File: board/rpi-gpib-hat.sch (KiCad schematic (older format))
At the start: 6 parts, among them J1 RPI_GPIO, J2 GPIB

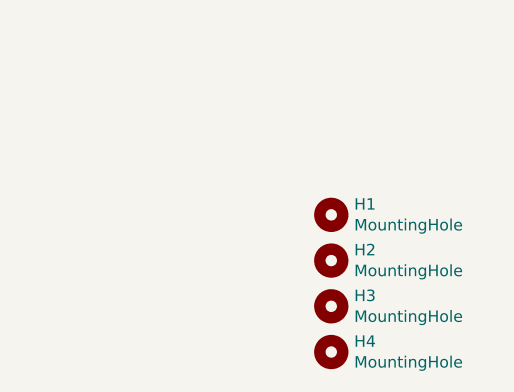
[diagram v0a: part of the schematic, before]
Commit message: Fix mounting holes to meet uHat spec.
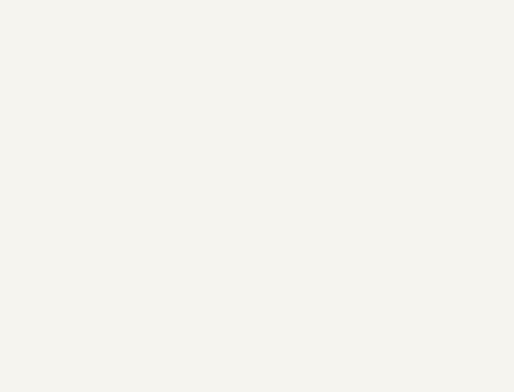
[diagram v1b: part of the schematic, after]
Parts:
- removed H1, H2, H3, H4: MountingHole, lib:MountingHole_2.7mm_M2.5_uHAT_RPi, symbol Mechanical:MountingHole
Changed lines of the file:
@@
 GPIO21
-$Comp
-L Mechanical:MountingHole H1
-U 1 1 5C7C4C81
-P 6150 6900
-F 0 "H1" H 6250 6946 50  0000 L CNN
-F 1 "MountingHole" H 6250 6855 50  0000 L CNN
-F 2 "lib:MountingHole_2.7mm_M2.5_uHAT_RPi" H 6150 6900 50  0001 C CNN
-F 3 "~" H 6150 6900 50  0001 C CNN
-	1    6150 6900
-	1    0    0    -1
-$EndComp
-$Comp
-L Mechanical:MountingHole H2
-U 1 1 5C7C7FBC
-P 6150 7100
-F 0 "H2" H 6250 7146 50  0000 L CNN
-F 1 "MountingHole" H 6250 7055 50  0000 L CNN
-F 2 "lib:MountingHole_2.7mm_M2.5_uHAT_RPi" H 6150 7100 50  0001 C CNN
-F 3 "~" H 6150 7100 50  0001 C CNN
-	1    6150 7100
-	1    0    0    -1
-$EndComp
-$Comp
-L Mechanical:MountingHole H3
-U 1 1 5C7C8014
-P 6150 7300
-F 0 "H3" H 6250 7346 50  0000 L CNN
-F 1 "MountingHole" H 6250 7255 50  0000 L CNN
-F 2 "lib:MountingHole_2.7mm_M2.5_uHAT_RPi" H 6150 7300 50  0001 C CNN
-F 3 "~" H 6150 7300 50  0001 C CNN
-	1    6150 7300
-	1    0    0    -1
-$EndComp
-$Comp
-L Mechanical:MountingHole H4
-U 1 1 5C7C8030
-P 6150 7500
-F 0 "H4" H 6250 7546 50  0000 L CNN
-F 1 "MountingHole" H 6250 7455 50  0000 L CNN
-F 2 "lib:MountingHole_2.7mm_M2.5_uHAT_RPi" H 6150 7500 50  0001 C CNN
-F 3 "~" H 6150 7500 50  0001 C CNN
-	1    6150 7500
-	1    0    0    -1
-$EndComp
 $Comp
 L Connector_Generic:Conn_02x12_Top_Bottom J2

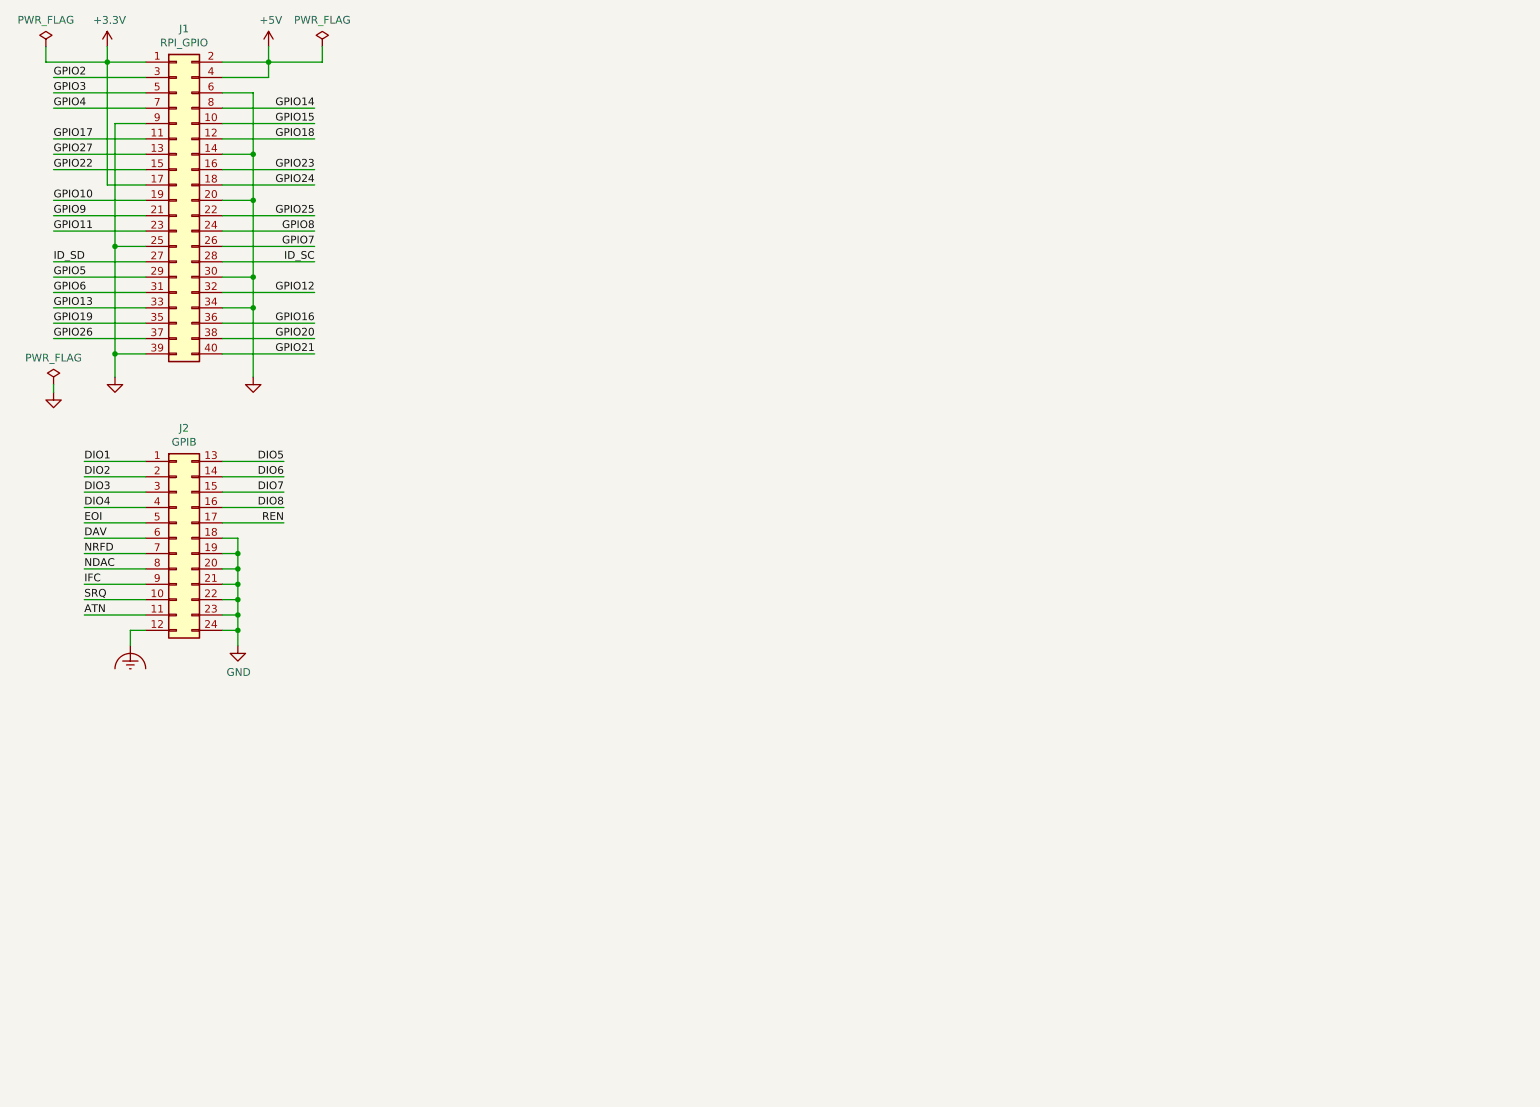
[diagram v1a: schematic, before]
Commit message: Add GPIB transceivers and ident EEPROM.
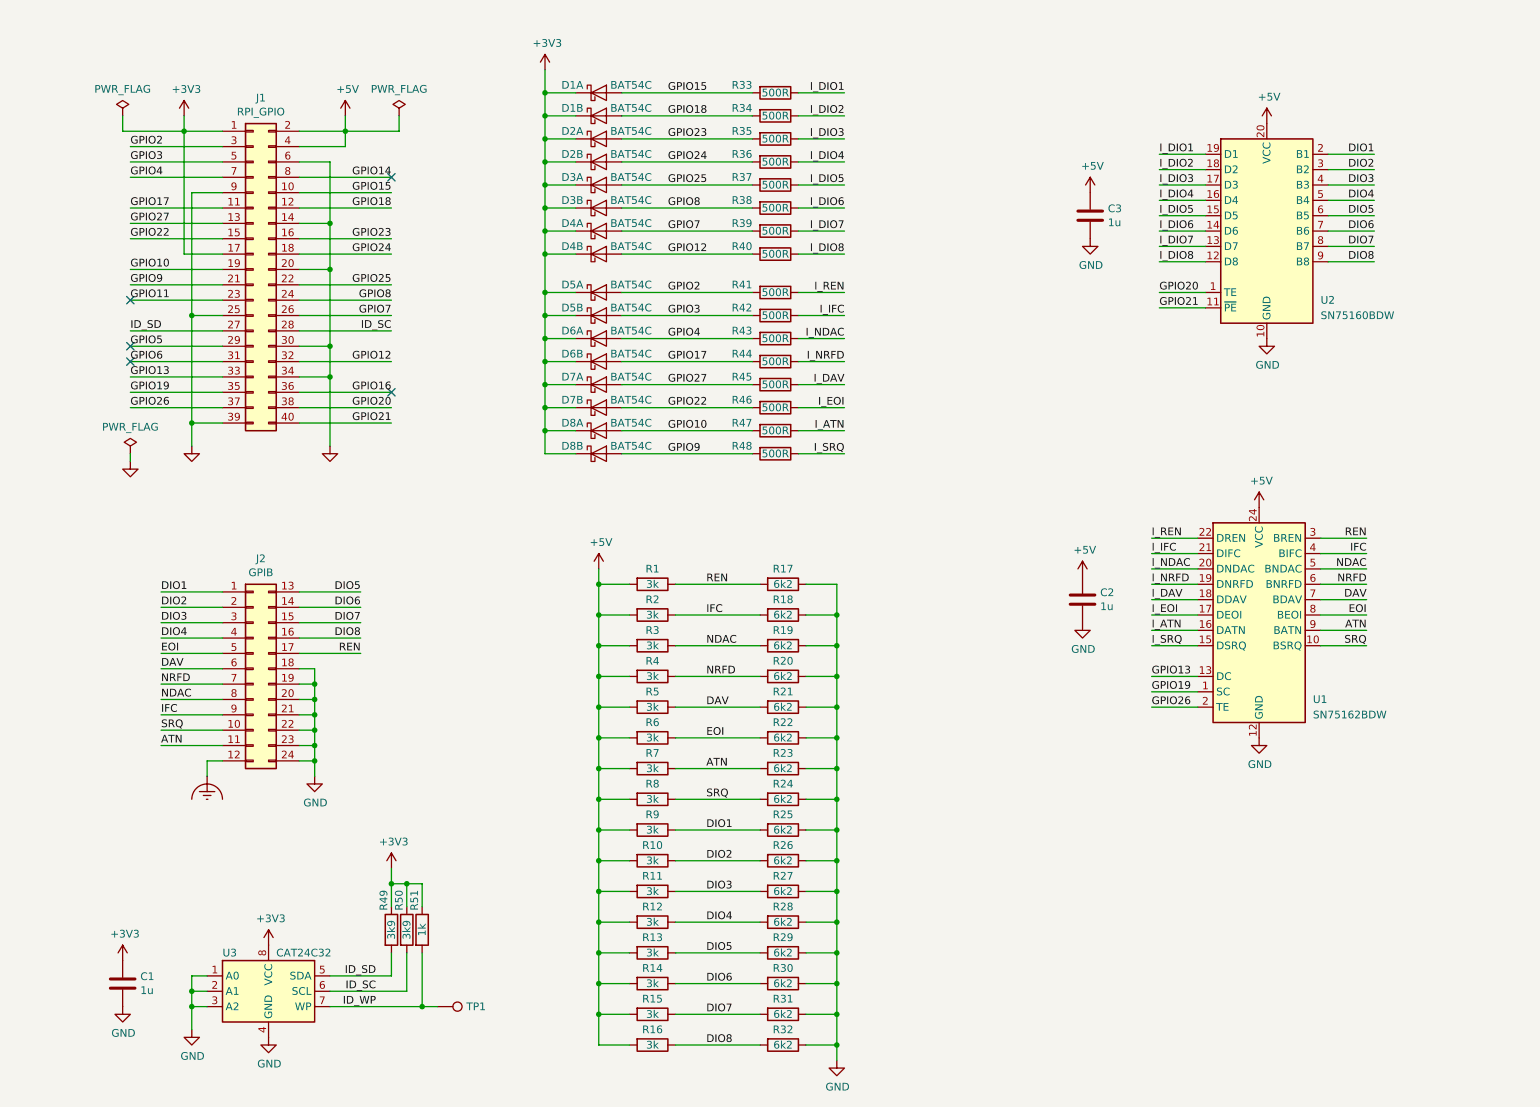
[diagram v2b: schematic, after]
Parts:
- added C1, C2, C3: 1u, Capacitor_SMD:C_0805_2012Metric, symbol Device:C
- added D1, D2, D3, D4, D5, D6, D7, D8: BAT54C, Package_TO_SOT_SMD:SOT-23, symbol local:D_Schottky_x2_KCom_AAK_Split
- added R1, R10, R11, R12, R13, R14, R15, R16, R2, R3, R4, R5, R6, R7, R8, R9: 3k, Resistor_SMD:R_0805_2012Metric, symbol Device:R
- added R17, R18, R19, R20, R21, R22, R23, R24, R25, R26, R27, R28, R29, R30, R31, R32: 6k2, Resistor_SMD:R_0805_2012Metric, symbol Device:R
- added R33, R34, R35, R36, R37, R38, R39, R40, R41, R42, R43, R44, R45, R46, R47, R48: 500R, Resistor_SMD:R_0805_2012Metric, symbol Device:R
- added R49, R50: 3k9, Resistor_SMD:R_0805_2012Metric, symbol Device:R
- added R51: 1k, Resistor_SMD:R_0805_2012Metric, symbol Device:R
- added TP1: TestPoint, TestPoint:TestPoint_Pad_D1.0mm, symbol Connector:TestPoint
- added U1: SN75162BDW, Package_SO:SOIC-24W_7.5x15.4mm_P1.27mm, symbol local:SN75162BDW
- added U2: SN75160BDW, Package_SO:SOIC-20W_7.5x12.8mm_P1.27mm, symbol Interface:SN75160BDW
- added U3: CAT24C32, Package_SO:SOIC-8_3.9x4.9mm_P1.27mm, symbol Memory_EEPROM:CAT24C128
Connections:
- net +3V3: now also C1.1, D1.3 (K), D1.3 (K), D2.3 (K), D2.3 (K), D3.3 (K), D3.3 (K), D4.3 (K), D4.3 (K), D5.3 (K), D5.3 (K), D6.3 (K), D6.3 (K), D7.3 (K), D7.3 (K), D8.3 (K), D8.3 (K), R49.1, R50.1, R51.1, U3.8 (VCC)
- net +5V: now also C2.1, C3.1, R1.2, R10.2, R11.2, R12.2, R13.2, R14.2, R15.2, R16.2, R2.2, R3.2, R4.2, R5.2, R6.2, R7.2, R8.2, R9.2, U1.24 (VCC), U2.20 (VCC)
- net ATN: now also R23.2, R7.1, U1.9 (BATN)
- net DAV: now also R21.2, R5.1, U1.7 (BDAV)
- net DIO1: now also R25.2, R9.1, U2.2 (B1)
- net DIO2: now also R10.1, R26.2, U2.3 (B2)
- net DIO3: now also R11.1, R27.2, U2.4 (B3)
- net DIO4: now also R12.1, R28.2, U2.5 (B4)
- net DIO5: now also R13.1, R29.2, U2.6 (B5)
- net DIO6: now also R14.1, R30.2, U2.7 (B6)
- net DIO7: now also R15.1, R31.2, U2.8 (B7)
- net DIO8: now also R16.1, R32.2, U2.9 (B8)
- net EOI: now also R22.2, R6.1, U1.8 (BEOI)
- net GND: now also C1.2, C2.2, C3.2, R17.1, R18.1, R19.1, R20.1, R21.1, R22.1, R23.1, R24.1, R25.1, R26.1, R27.1, R28.1, R29.1, R30.1, R31.1, R32.1, U1.12 (GND), U2.10 (GND), U3.1 (A0), U3.2 (A1), U3.3 (A2), U3.4 (GND)
- net GPIO10: now also D8.1 (A), R47.2
- net GPIO12: now also D4.2 (A), R40.2
- net GPIO13: now also U1.13 (DC)
- net GPIO15: now also D1.1 (A), R33.2
- net GPIO17: now also D6.2 (A), R44.2
- net GPIO18: now also D1.2 (A), R34.2
- net GPIO19: now also U1.1 (SC)
- net GPIO2: now also D5.1 (A), R41.2
- net GPIO20: now also U2.1 (TE)
- net GPIO21: now also U2.11 (~PE)
- net GPIO22: now also D7.2 (A), R46.2
- net GPIO23: now also D2.1 (A), R35.2
- net GPIO24: now also D2.2 (A), R36.2
- net GPIO25: now also D3.1 (A), R37.2
- net GPIO26: now also U1.2 (TE)
- net GPIO27: now also D7.1 (A), R45.2
- net GPIO3: now also D5.2 (A), R42.2
- net GPIO4: now also D6.1 (A), R43.2
- net GPIO7: now also D4.1 (A), R39.2
- net GPIO8: now also D3.2 (A), R38.2
- net GPIO9: now also D8.2 (A), R48.2
- net ID_SC: now also R50.2, U3.6 (SCL)
- net ID_SD: now also R49.2, U3.5 (SDA)
- net IFC: now also R18.2, R2.1, U1.4 (BIFC)
- net NDAC: now also R19.2, R3.1, U1.5 (BNDAC)
- net NRFD: now also R20.2, R4.1, U1.6 (BNRFD)
- net REN: now also R1.1, R17.2, U1.3 (BREN)
- net SRQ: now also R24.2, R8.1, U1.10 (BSRQ)
- new net ID_WP: R51.2, TP1.1, U3.7 (WP)
- new net I_ATN: R47.1, U1.16 (DATN)
- new net I_DAV: R45.1, U1.18 (DDAV)
- new net I_DIO1: R33.1, U2.19 (D1)
- new net I_DIO2: R34.1, U2.18 (D2)
- new net I_DIO3: R35.1, U2.17 (D3)
- new net I_DIO4: R36.1, U2.16 (D4)
- new net I_DIO5: R37.1, U2.15 (D5)
- new net I_DIO6: R38.1, U2.14 (D6)
- new net I_DIO7: R39.1, U2.13 (D7)
- new net I_DIO8: R40.1, U2.12 (D8)
- new net I_EOI: R46.1, U1.17 (DEOI)
- new net I_IFC: R42.1, U1.21 (DIFC)
- new net I_NDAC: R43.1, U1.20 (DNDAC)
- new net I_NRFD: R44.1, U1.19 (DNRFD)
- new net I_REN: R41.1, U1.22 (DREN)
- new net I_SRQ: R48.1, U1.15 (DSRQ)
- no-connect marks 0 -> 5
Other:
- moved on the sheet: J1, J2

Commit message: Start laying out the PCB.
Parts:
- R1, R10, R11, R12, R13, R14, R15, R16, R17, R18, R19, R2, R20, R21, R22, R23, R24, R25, R26, R27, R28, R29, R3, R30, R31, R32, R33, R34, R35, R36, R37, R38, R39, R4, R40, R41, R42, R43, R44, R45, R46, R47, R48, R49, R5, R50, R51, R6, R7, R8, R9: footprint Resistor_SMD:R_0805_2012Metric -> Resistor_SMD:R_0402_1005Metric

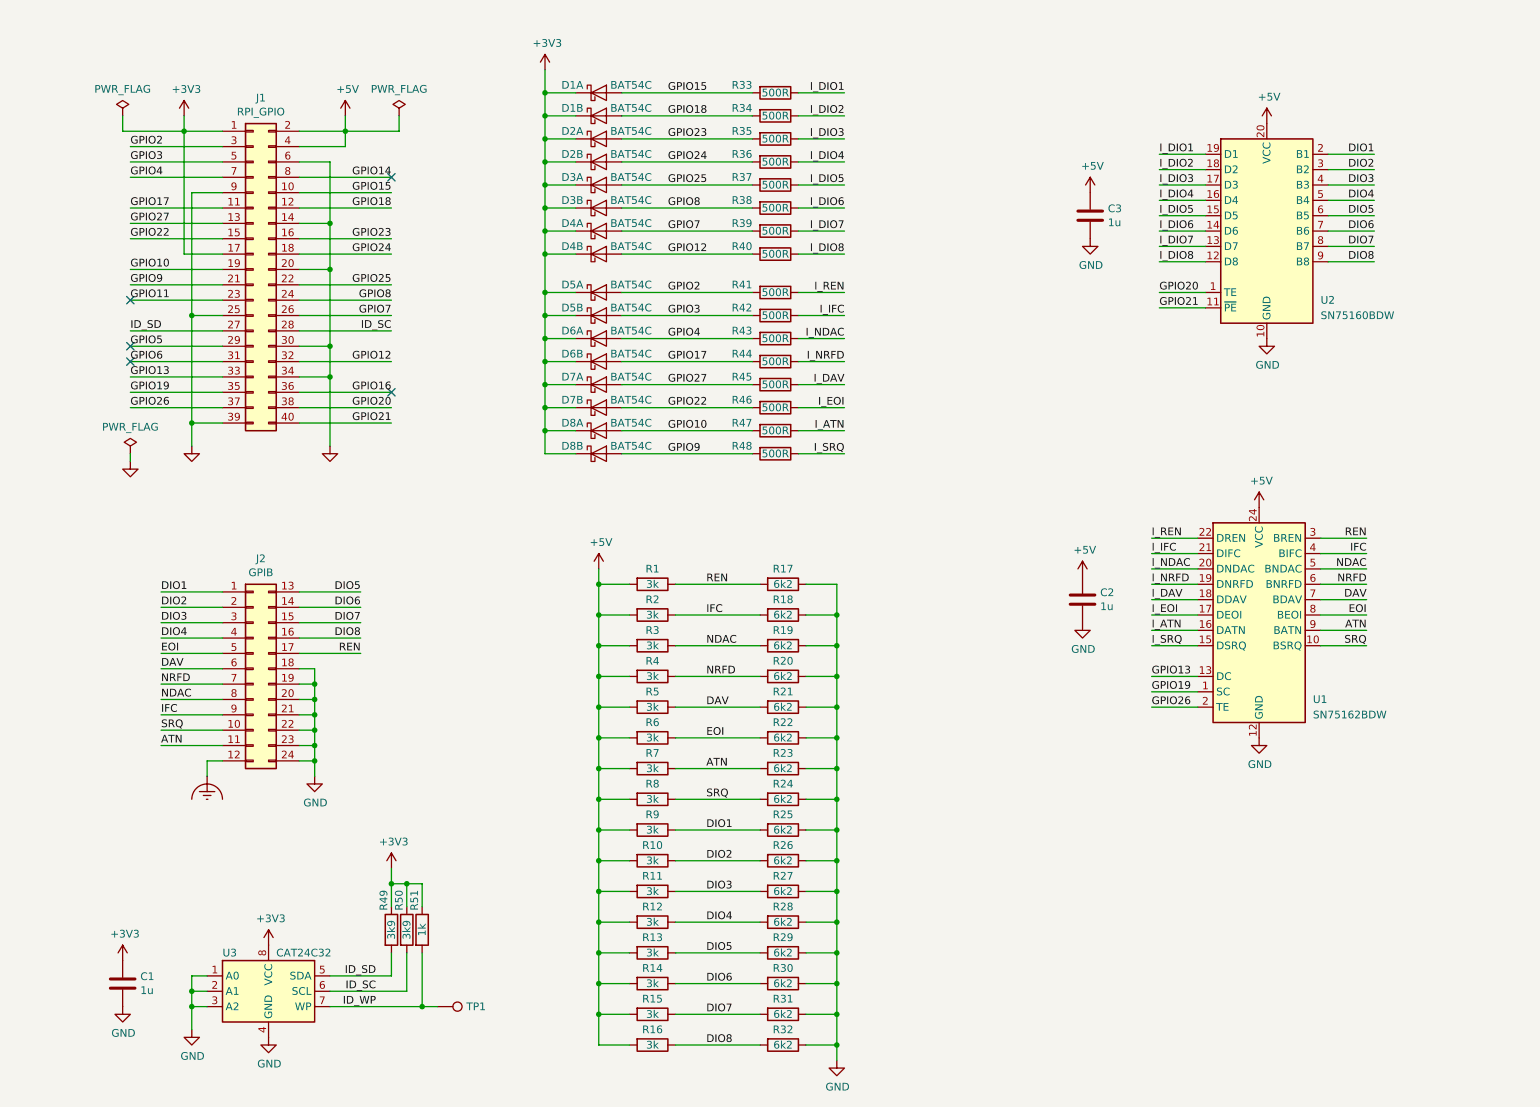
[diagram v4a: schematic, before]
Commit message: Add 2.5V regulator for diode clamps.
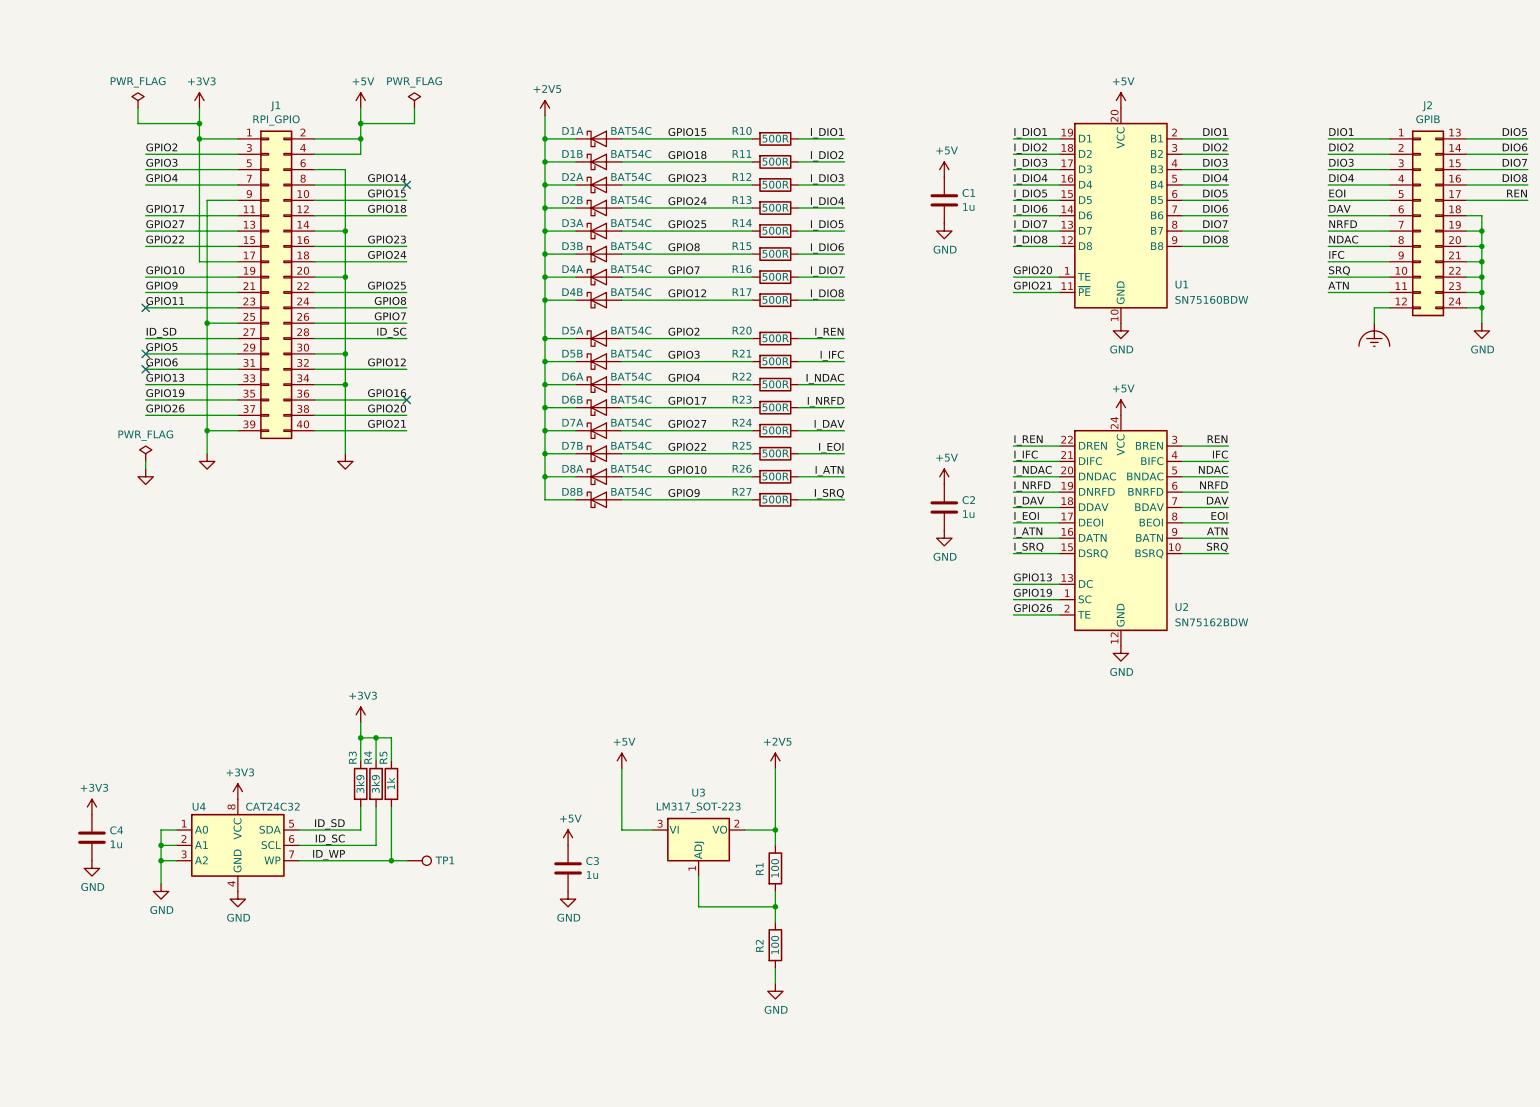
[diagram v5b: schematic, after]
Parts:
- removed R10, R11, R12, R13, R14, R15, R16, R3, R4, R5, R6, R7, R8, R9: 3k, Resistor_SMD:R_0402_1005Metric, symbol Device:R
- removed R17, R18, R19, R20, R21, R22, R23, R24, R25, R26, R27, R28, R29, R30, R31, R32: 6k2, Resistor_SMD:R_0402_1005Metric, symbol Device:R
- added C3: 1u, Capacitor_SMD:C_0805_2012Metric, symbol Device:C
- added U3: LM317_SOT-223, Package_TO_SOT_SMD:SOT-223-3_TabPin2, symbol Regulator_Linear:LM317_SOT-223
- R1, R2: value 3k -> 100
- renumbered C3 to C1, C1 to C4, R33 to R10, R34 to R11, R35 to R12, R36 to R13, R37 to R14, R38 to R15, R39 to R16, R40 to R17, R41 to R20, R42 to R21, R43 to R22, R44 to R23, R45 to R24, R46 to R25, R47 to R26, R48 to R27, R49 to R3, R50 to R4, R51 to R5, U2 to U1, U1 to U2, U3 to U4
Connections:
- net +3V3: no longer D1.3 (K), D1.3 (K), D2.3 (K), D2.3 (K), D3.3 (K), D3.3 (K), D4.3 (K), D4.3 (K), D5.3 (K), D5.3 (K), D6.3 (K), D6.3 (K), D7.3 (K), D7.3 (K), D8.3 (K), D8.3 (K)
- net +5V: now also C3.1, U3.3 (VI); no longer R1.2, R2.2
- net GND: now also R2.2, C3.2
- net IFC: no longer R2.1
- net REN: no longer R1.1
- new net: R1.2, R2.1, U3.1 (ADJ)
- new net +2V5: D1.3 (K), D1.3 (K), D2.3 (K), D2.3 (K), D3.3 (K), D3.3 (K), D4.3 (K), D4.3 (K), D5.3 (K), D5.3 (K), D6.3 (K), D6.3 (K), D7.3 (K), D7.3 (K), D8.3 (K), D8.3 (K), R1.1, U3.2 (VO)
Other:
- moved on the sheet: C1, C2, C4, D1A, D1B, D2A, D2B, D3A, D3B, D4A, D4B, D5A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

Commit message: Clean up routing.
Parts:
- removed C3: 1u, Capacitor_SMD:C_0805_2012Metric, symbol Device:C
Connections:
- net GPIO20: now also U1.11 (~PE); no longer U1.1 (TE)
- net GPIO21: now also U1.1 (TE); no longer U1.11 (~PE)
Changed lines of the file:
@@
 	7350 2500 7050 2500
 Text Label 7050 2400 0    50   ~ 0
+GPIO21
+Text Label 7050 2500 0    50   ~ 0
 GPIO20
-Text Label 7050 2500 0    50   ~ 0
-GPIO21
 Text Label 7050 4400 0    50   ~ 0
 GPIO13
@@
 Wire Wire Line
 	5500 7000 5500 6900
-$Comp
-L Device:C C3
-U 1 1 61F8EFD2
-P 4150 6250
-F 0 "C3" H 4265 6296 50  0000 L CNN
-F 1 "1u" H 4265 6205 50  0000 L CNN
-F 2 "Capacitor_SMD:C_0805_2012Metric" H 4188 6100 50  0001 C CNN
-F 3 "~" H 4150 6250 50  0001 C CNN
-	1    4150 6250
-	1    0    0    -1
-$EndComp
-$Comp
-L power:+5V #PWR015
-U 1 1 61F8F660
-P 4150 6100
-F 0 "#PWR015" H 4150 5950 50  0001 C CNN
-F 1 "+5V" H 4165 6273 50  0000 C CNN
-F 2 "" H 4150 6100 50  0001 C CNN
-F 3 "" H 4150 6100 50  0001 C CNN
-	1    4150 6100
-	1    0    0    -1
-$EndComp
-$Comp
-L power:GND #PWR016
-U 1 1 61F8F66A
-P 4150 6400
-F 0 "#PWR016" H 4150 6150 50  0001 C CNN
-F 1 "GND" H 4155 6227 50  0000 C CNN
-F 2 "" H 4150 6400 50  0001 C CNN
-F 3 "" H 4150 6400 50  0001 C CNN
-	1    4150 6400
-	1    0    0    -1
-$EndComp
 Wire Wire Line
 	1750 1400 1750 1300
